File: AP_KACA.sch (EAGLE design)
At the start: 28 parts, among them IC1 REG710XX-3.3, J1 FTDI_DEVICE, M1 WIRELESS-NRF24L01, Q1 BSS123, Q2 BSS123, Q3 BSS123, Q4 BSS123, U3 GY-521MPU6050, Y1 8MHz

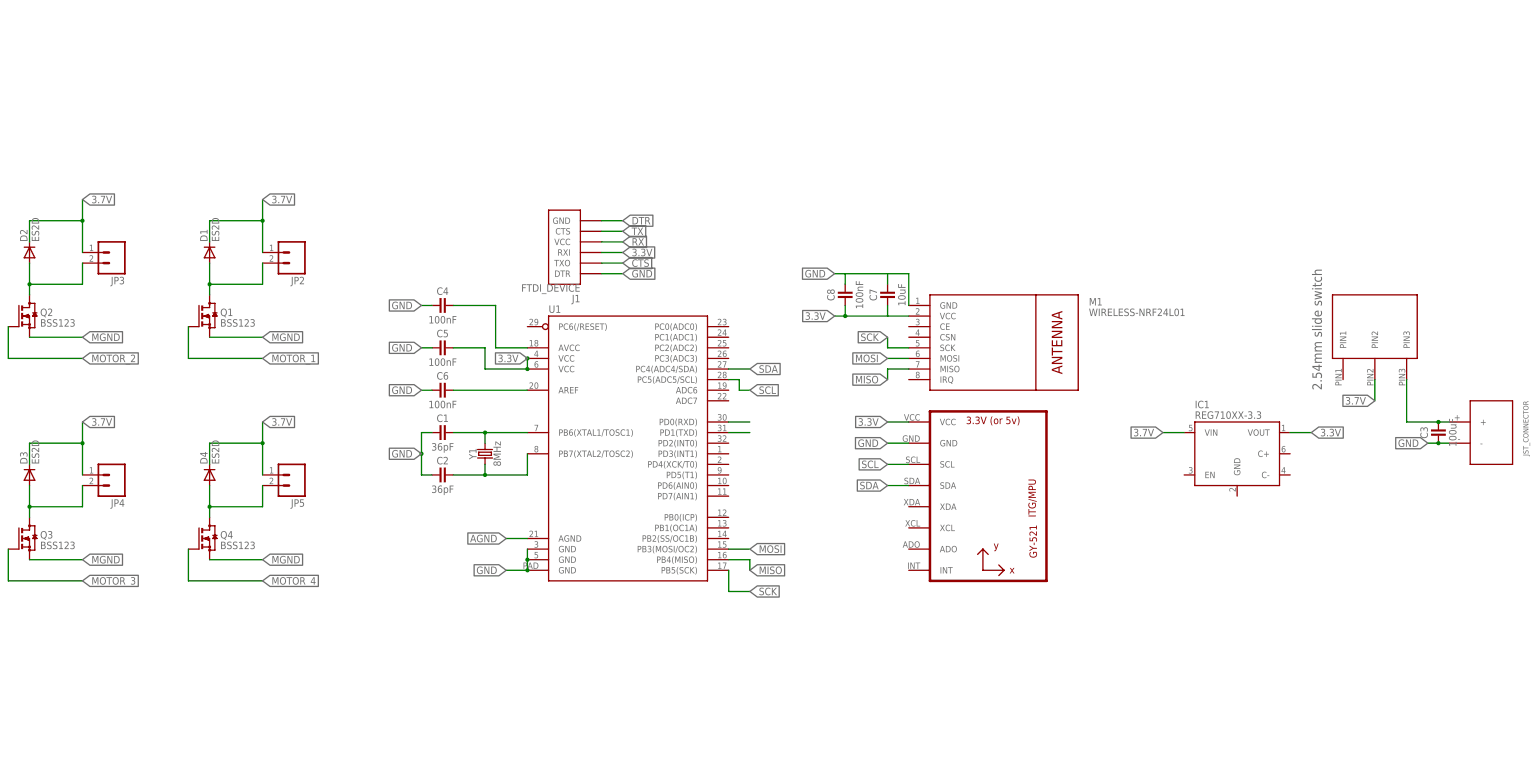
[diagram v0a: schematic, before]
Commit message: Added some passives
added some capacitors and resistors
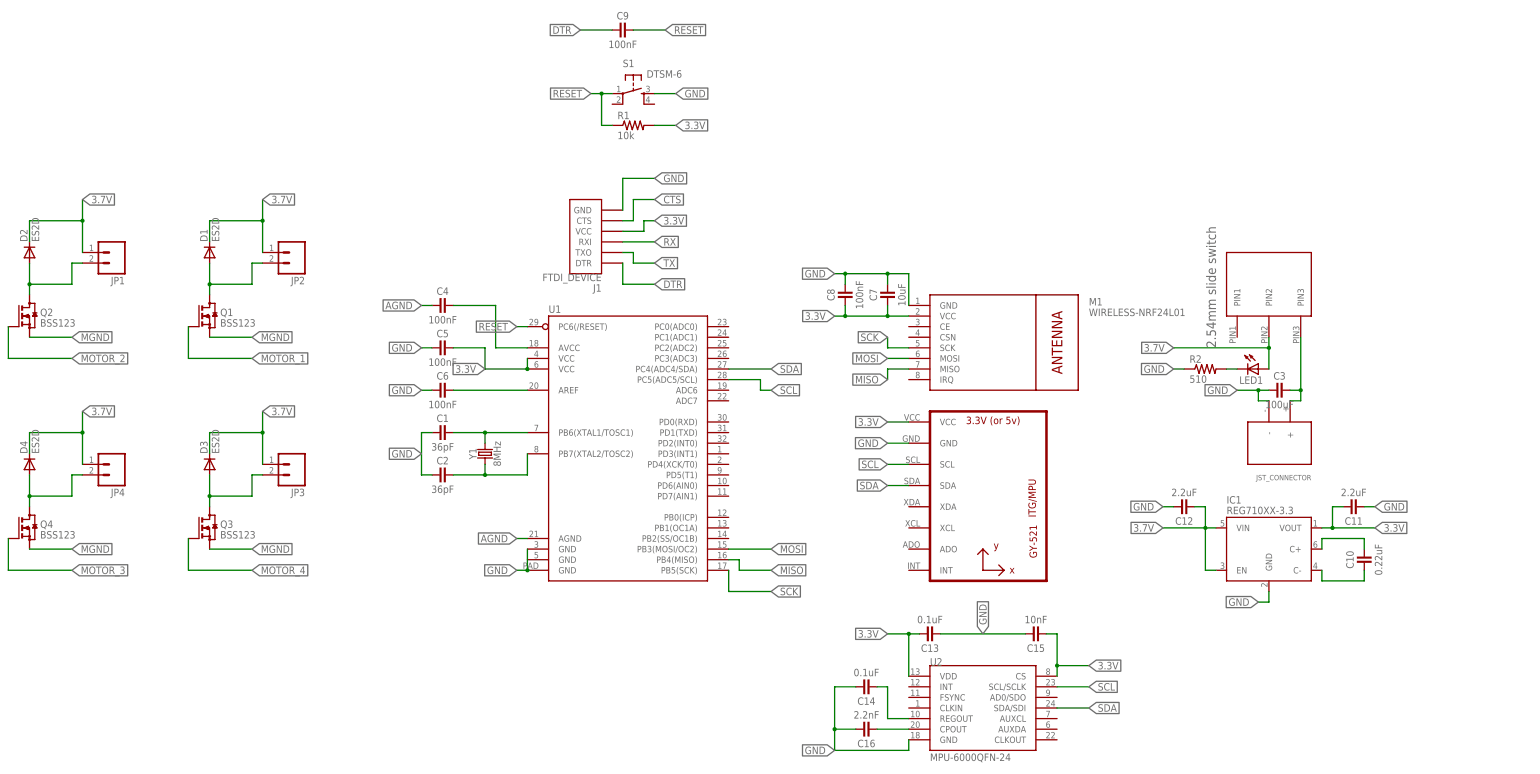
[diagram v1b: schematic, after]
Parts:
- removed JP5: (no value), SparkFun:M02PTH3
- added C10: 0.22uF, we-rcl:CAPACITOR-1206
- added C11, C12: 2.2uF, we-rcl:CAPACITOR-1206
- added C13, C14: 0.1uF, we-rcl:CAPACITOR-1206
- added C15: 10nF, we-rcl:CAPACITOR-1206
- added C16: 2.2nF, we-rcl:CAPACITOR-1206
- added C9: 100nF, we-rcl:CAPACITOR-0603
- added JP1: (no value), SparkFun:M02PTH3
- added LED1: (no value), eagle-ltspice:LED_ESML0603
- added R1: 10k, SparkFun-Resistors:10.5KOHM1/10W1%(0603)
- added R2: 510, SparkFun-Resistors:10.5KOHM1/10W1%(0603)
- added S1: DTSM-6, switch-tact:DTSM-6
- added U2: MPU-6000QFN-24, SparkFun-Sensors:MPU-6000QFN-24
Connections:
- new net N$13: C14.1, U2.REGOUT
- new net N$14: C16.1, U2.CPOUT
- new net N$5: LED1.C, R2.2
- new net RESET: C9.2, R1.1, S1.1, U1.PC6(/RESET)
- net 3.3V: now also C11.2, C13.2, C15.1, J1.VCC, R1.2, U2.CS, U2.VDD; no longer J1.RXI
- net 3.7V: now also C12.1, IC1.EN, JP1.1, LED1.A; no longer JP5.1
- net AGND: now also C4.1
- net CTS: now also J1.CTS; no longer J1.TXO
- net DTR: now also C9.1, J1.DTR; no longer J1.GND
- net GND: now also C11.1, C12.2, C13.1, C14.2, C15.2, C16.2, IC1.GND, J1.GND, R2.1, S1.3, U2.GND; no longer C4.1, J1.DTR, U1.GND@5
- net MOTOR_3: now also Q4.G; no longer Q3.G
- net MOTOR_4: now also Q3.G; no longer Q4.G
- net N$1: now also JP1.2; no longer JP3.2
- net N$10: now also C10.2, IC1.C+; no longer U1.PD1(TXD)
- net N$11: now also C10.1, IC1.C-; no longer U1.PD0(RXD)
- net N$3: now also JP3.2; no longer JP4.2
- net N$4: now also JP4.2; no longer JP5.2
- net RX: now also J1.RXI; no longer J1.VCC
- net SCL: now also U2.SCL/SCLK
- net SDA: now also U2.SDA/SDI
- net TX: now also J1.TXO; no longer J1.CTS
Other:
- moved on the sheet: C3, D3, D4, IC1, J1, JP3, JP4, Q3, Q4

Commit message: kind of finished quadcopter schematic
added indicatory leds, voltage divider, pull down resistors for motors
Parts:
- added LED2, LED3, LED4: (no value), eagle-ltspice:LED_ESML0603
- added R10, R11, R3, R4, R5, R6: 36k, SparkFun-Resistors:10.5KOHM1/10W1%(0603)
- added R7, R8, R9: 510, SparkFun-Resistors:10.5KOHM1/10W1%(0603)
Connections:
- new net LED_1: LED2.A, U1.PD7(AIN1)
- new net LED_2: LED3.A, U1.PB0(ICP)
- new net LED_3: LED4.A, U1.PB2(SS/OC1B)
- new net N$15: LED3.C, R8.1
- new net N$16: LED2.C, R7.1
- new net N$17: LED4.C, R9.1
- new net V_READER: R10.1, R11.2, U1.PC0(ADC0)
- net 3.7V: now also R10.2
- net GND: now also R11.1, R7.2, R8.2, R9.2
- net MGND: now also R3.2, R4.2, R5.2, R6.2
- net MOTOR_1: now also R3.1, U1.PD3(INT1)
- net MOTOR_2: now also R4.1, U1.PD5(T1)
- net MOTOR_3: now also R6.1, U1.PD6(AIN0)
- net MOTOR_4: now also R5.1, U1.PB1(OC1A)
- net RX: now also U1.PD1(TXD)
- net TX: now also U1.PD0(RXD)
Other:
- moved on the sheet: D2, D3, D4, JP1, JP3, JP4, Q2, Q3, Q4

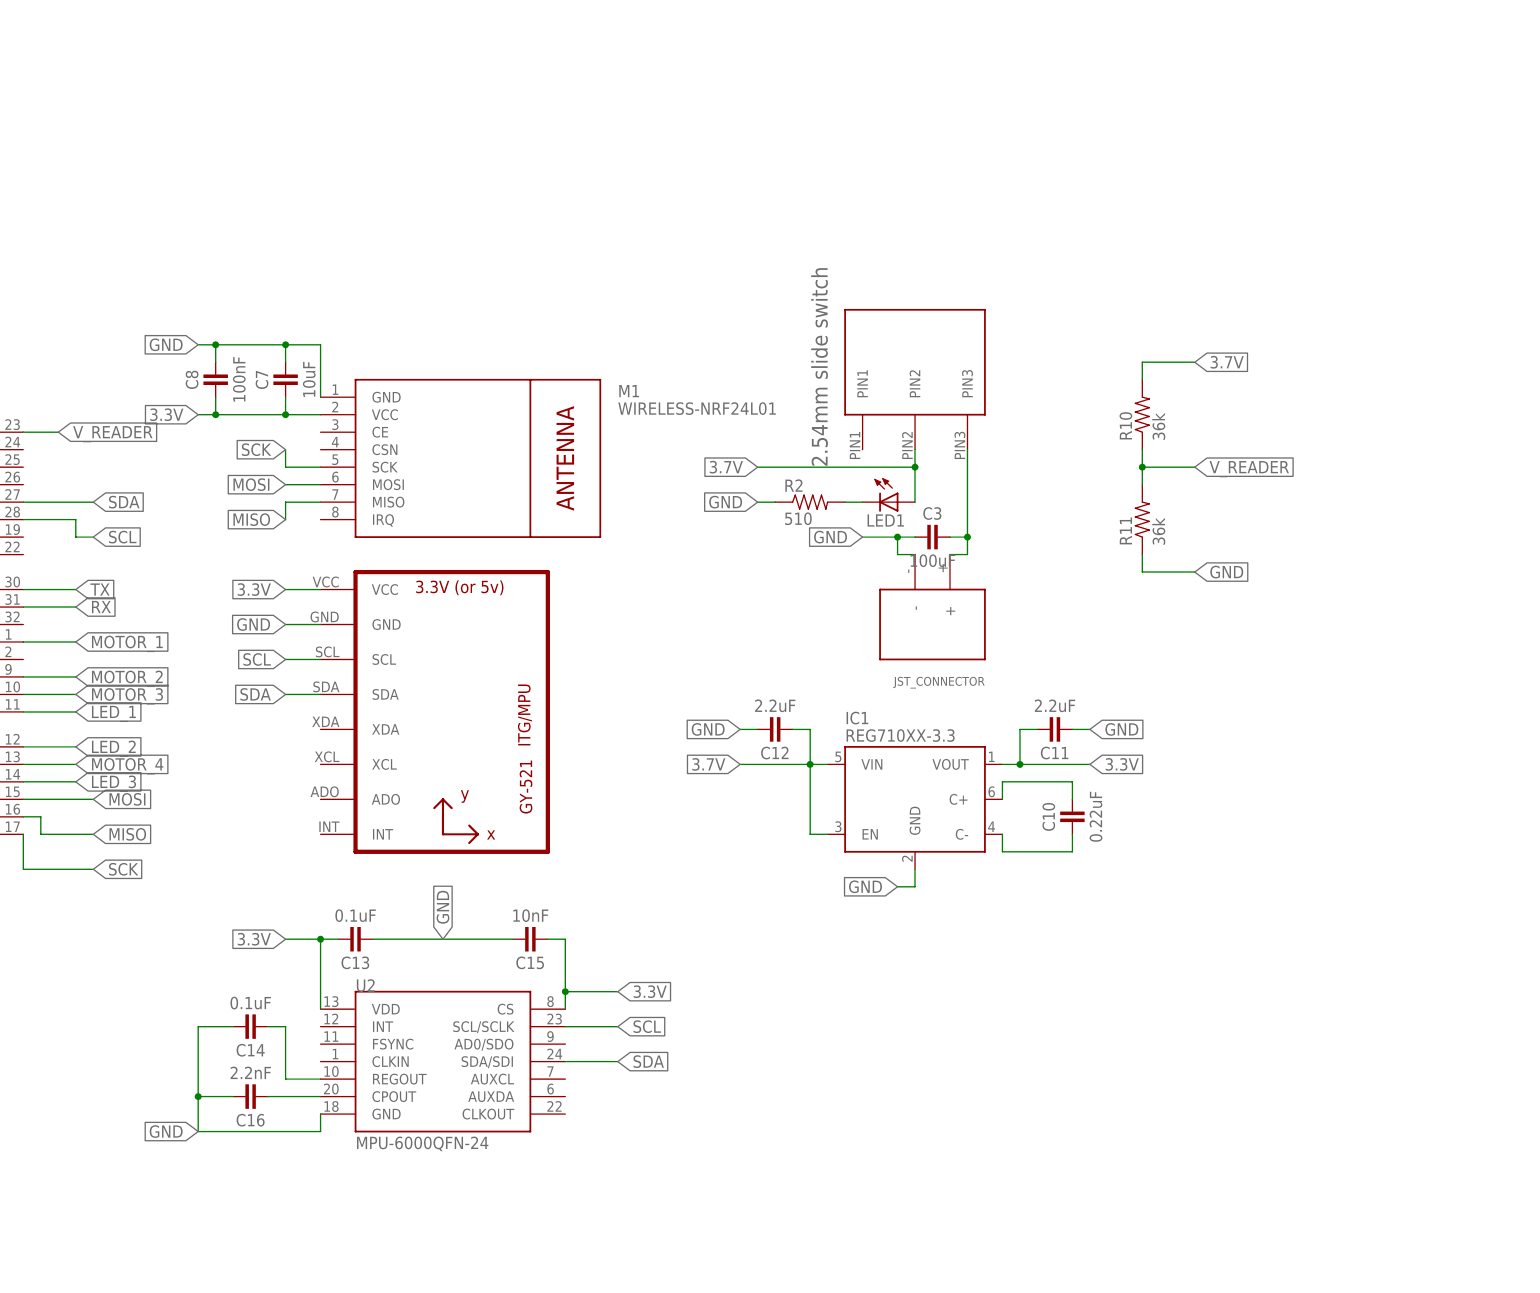
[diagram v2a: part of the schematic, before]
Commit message: added missing components
there were some missing labels and parts of the schematic
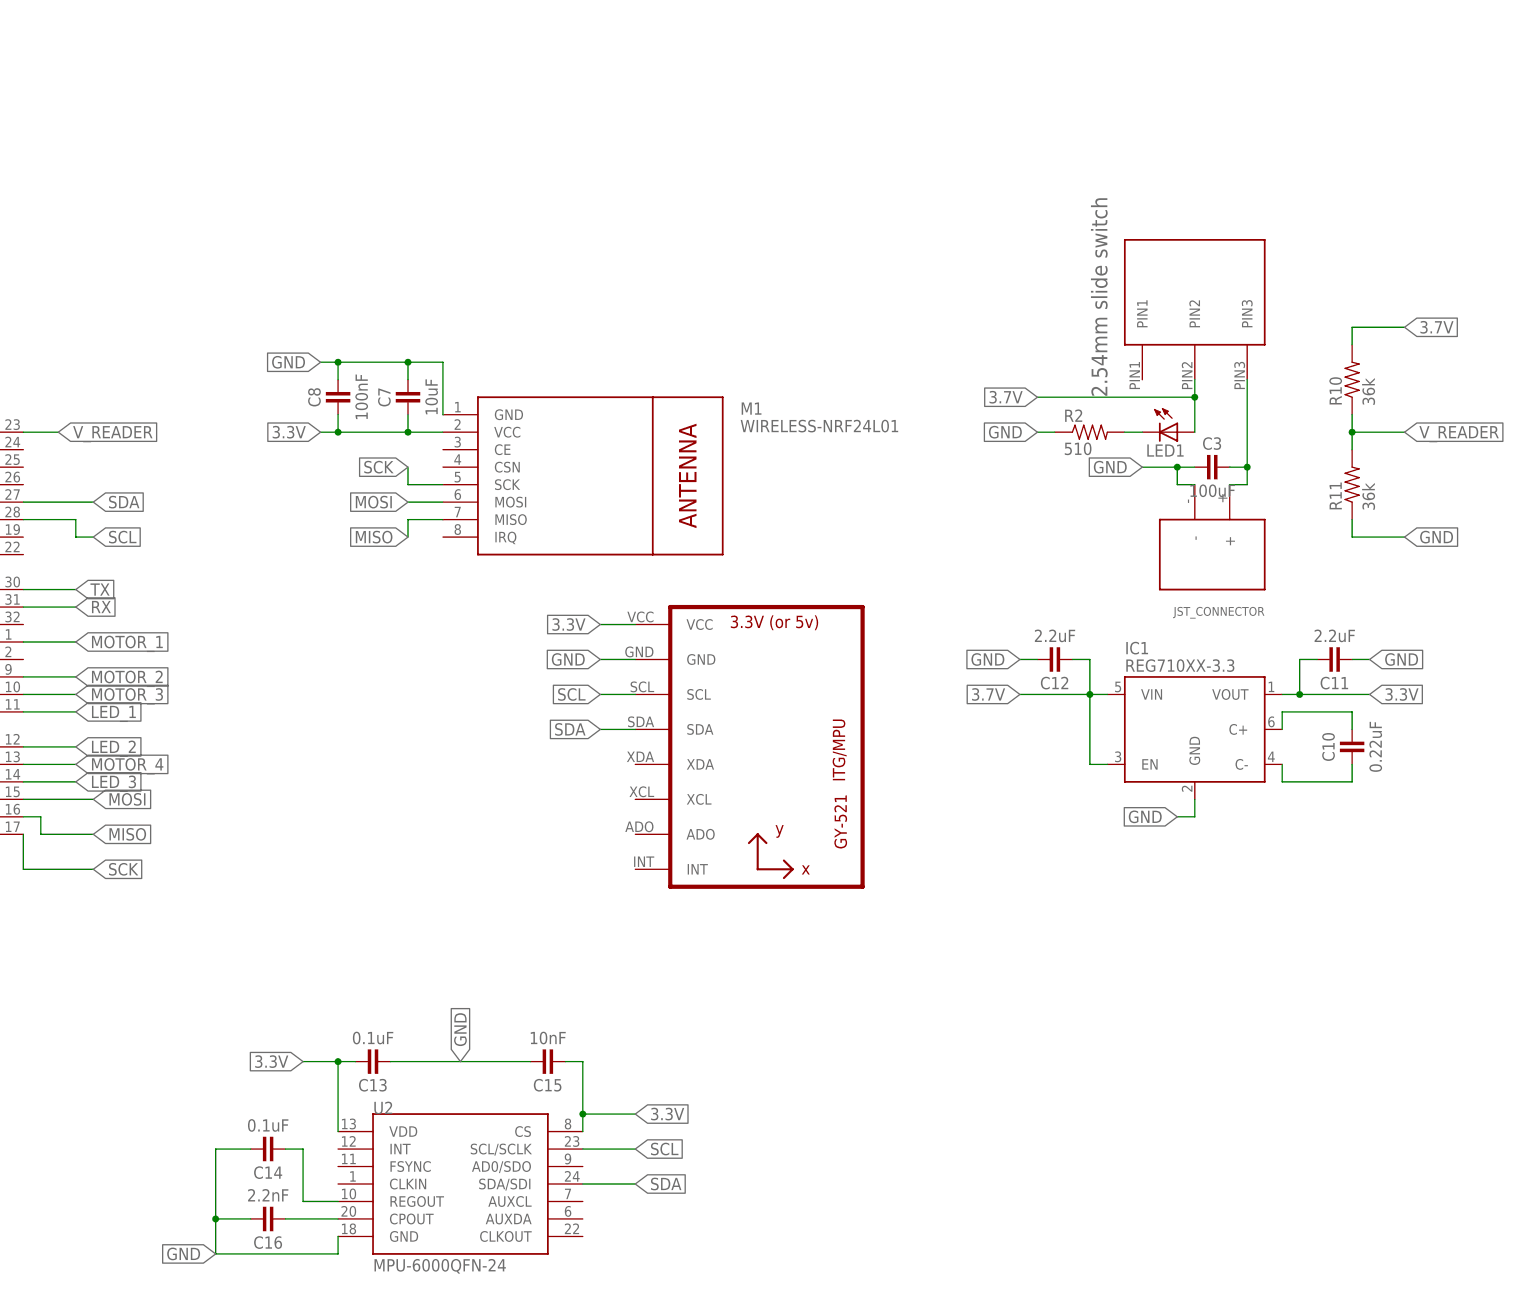
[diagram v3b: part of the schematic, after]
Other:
- moved on the sheet: C10, C11, C12, C13, C14, C15, C16, C3, C7, C8, IC1, LED1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
